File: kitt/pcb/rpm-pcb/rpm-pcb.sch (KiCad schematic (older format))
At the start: 155 parts, among them J1 Screw_Terminal_01x02, J2 Screw_Terminal_01x03, Q1 NDP6020P, Q2 NDP6020P, Q3 NDP6020P, Q4 NDP6020P, Q5 NDP6020P, Q6 NDP6020P, U1 TLC5940NT, U2 TLC5940NT, U3 TLC5940NT, U4 TLC5940NT, U5 TLC5940NT, U6 TLC5940NT, U7 TLC5940NT, U8 TLC5940NT, U9 TLC5940NT

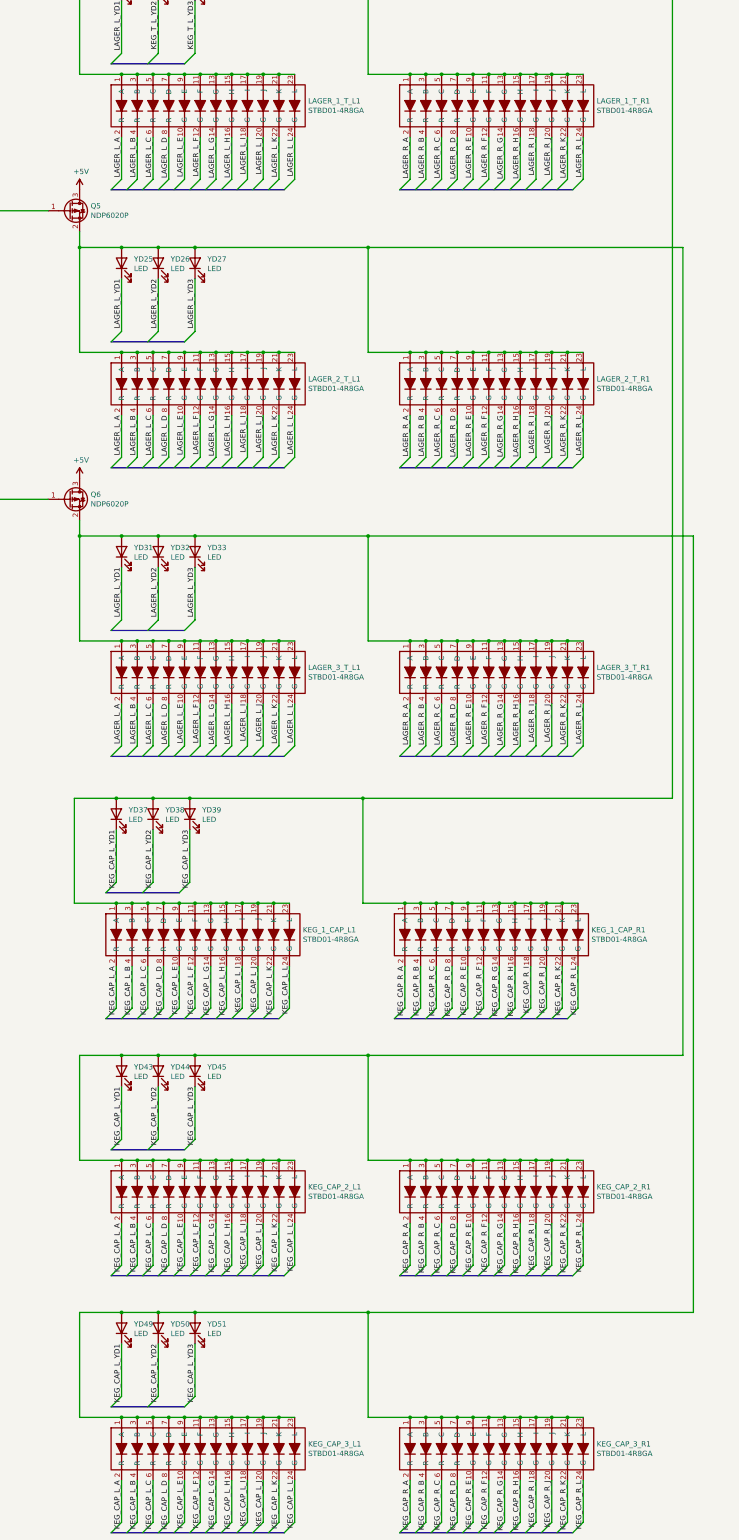
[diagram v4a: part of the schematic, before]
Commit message: fixed colors on bar displays
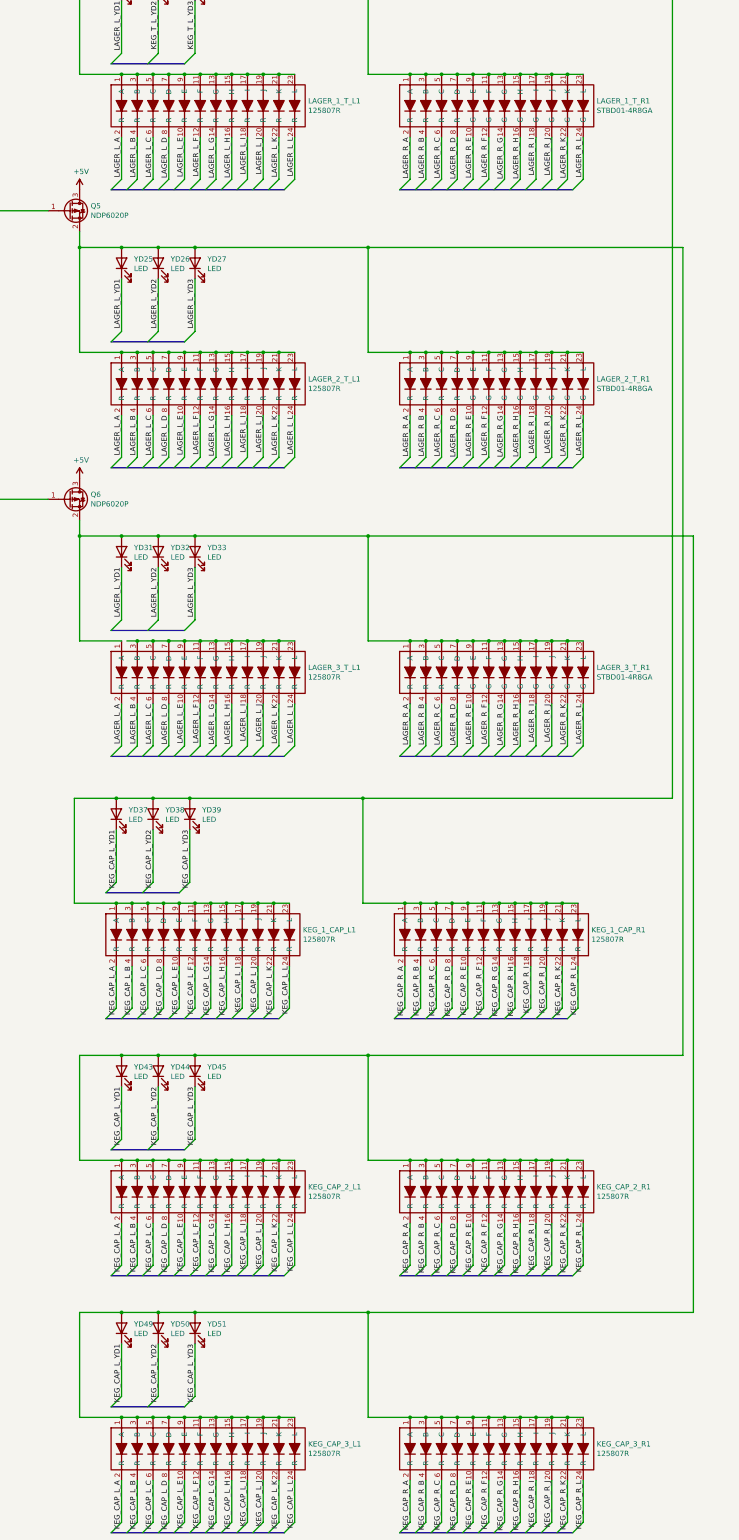
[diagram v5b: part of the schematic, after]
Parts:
- removed KEG_1_CAP_L1, KEG_1_CAP_R1, KEG_CAP_2_L1, KEG_CAP_2_R1, KEG_CAP_3_L1, KEG_CAP_3_R1, LAGER_1_T_L1, LAGER_2_T_L1, LAGER_3_T_L1: STBD01-4R8GA, symbol KITT-Symbols:STBD01-4R8GA
- added KEG_1_CAP_L1, KEG_1_CAP_R1, KEG_CAP_2_L1, KEG_CAP_2_R1, KEG_CAP_3_L1, KEG_CAP_3_R1, LAGER_1_T_L1, LAGER_2_T_L1, LAGER_3_T_L1: 125807R, symbol KITT-Symbols:125807R
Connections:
- net KEG_CAP_L_A: now also KEG_1_CAP_L1.2 (R), KEG_CAP_2_L1.2 (R), KEG_CAP_3_L1.2 (R)
- net KEG_CAP_L_B: now also KEG_1_CAP_L1.4 (R), KEG_CAP_2_L1.4 (R), KEG_CAP_3_L1.4 (R)
- net KEG_CAP_L_C: now also KEG_1_CAP_L1.6 (R), KEG_CAP_2_L1.6 (R), KEG_CAP_3_L1.6 (R)
- net KEG_CAP_L_D: now also KEG_1_CAP_L1.8 (R), KEG_CAP_2_L1.8 (R), KEG_CAP_3_L1.8 (R)
- net KEG_CAP_L_E: now also KEG_1_CAP_L1.10 (R), KEG_CAP_2_L1.10 (R), KEG_CAP_3_L1.10 (R)
- net KEG_CAP_L_F: now also KEG_1_CAP_L1.12 (R), KEG_CAP_2_L1.12 (R), KEG_CAP_3_L1.12 (R)
- net KEG_CAP_L_G: now also KEG_1_CAP_L1.14 (R), KEG_CAP_2_L1.14 (R), KEG_CAP_3_L1.14 (R)
- net KEG_CAP_L_H: now also KEG_1_CAP_L1.16 (R), KEG_CAP_2_L1.16 (R), KEG_CAP_3_L1.16 (R)
- net KEG_CAP_L_I: now also KEG_1_CAP_L1.18 (R), KEG_CAP_2_L1.18 (R), KEG_CAP_3_L1.18 (R)
- net KEG_CAP_L_J: now also KEG_1_CAP_L1.20 (R), KEG_CAP_2_L1.20 (R), KEG_CAP_3_L1.20 (R)
- net KEG_CAP_L_K: now also KEG_1_CAP_L1.22 (R), KEG_CAP_2_L1.22 (R), KEG_CAP_3_L1.22 (R)
- net KEG_CAP_L_L: now also KEG_1_CAP_L1.24 (R), KEG_CAP_2_L1.24 (R), KEG_CAP_3_L1.24 (R)
- net KEG_CAP_R_A: now also KEG_1_CAP_R1.2 (R), KEG_CAP_2_R1.2 (R), KEG_CAP_3_R1.2 (R)
- net KEG_CAP_R_B: now also KEG_1_CAP_R1.4 (R), KEG_CAP_2_R1.4 (R), KEG_CAP_3_R1.4 (R)
- net KEG_CAP_R_C: now also KEG_1_CAP_R1.6 (R), KEG_CAP_2_R1.6 (R), KEG_CAP_3_R1.6 (R)
- net KEG_CAP_R_D: now also KEG_1_CAP_R1.8 (R), KEG_CAP_2_R1.8 (R), KEG_CAP_3_R1.8 (R)
- net KEG_CAP_R_E: now also KEG_1_CAP_R1.10 (R), KEG_CAP_2_R1.10 (R), KEG_CAP_3_R1.10 (R)
- net KEG_CAP_R_F: now also KEG_1_CAP_R1.12 (R), KEG_CAP_2_R1.12 (R), KEG_CAP_3_R1.12 (R)
- net KEG_CAP_R_G: now also KEG_1_CAP_R1.14 (R), KEG_CAP_2_R1.14 (R), KEG_CAP_3_R1.14 (R)
- net KEG_CAP_R_H: now also KEG_1_CAP_R1.16 (R), KEG_CAP_2_R1.16 (R), KEG_CAP_3_R1.16 (R)
- net KEG_CAP_R_I: now also KEG_1_CAP_R1.18 (R), KEG_CAP_2_R1.18 (R), KEG_CAP_3_R1.18 (R)
- net KEG_CAP_R_J: now also KEG_1_CAP_R1.20 (R), KEG_CAP_2_R1.20 (R), KEG_CAP_3_R1.20 (R)
- net KEG_CAP_R_K: now also KEG_1_CAP_R1.22 (R), KEG_CAP_2_R1.22 (R), KEG_CAP_3_R1.22 (R)
- net KEG_CAP_R_L: now also KEG_1_CAP_R1.24 (R), KEG_CAP_2_R1.24 (R), KEG_CAP_3_R1.24 (R)
- net LAGER_L_A: now also LAGER_1_T_L1.2 (R), LAGER_2_T_L1.2 (R), LAGER_3_T_L1.2 (R)
- net LAGER_L_B: now also LAGER_1_T_L1.4 (R), LAGER_2_T_L1.4 (R), LAGER_3_T_L1.4 (R)
- net LAGER_L_C: now also LAGER_1_T_L1.6 (R), LAGER_2_T_L1.6 (R), LAGER_3_T_L1.6 (R)
- net LAGER_L_D: now also LAGER_1_T_L1.8 (R), LAGER_2_T_L1.8 (R), LAGER_3_T_L1.8 (R)
- net LAGER_L_E: now also LAGER_1_T_L1.10 (R), LAGER_2_T_L1.10 (R), LAGER_3_T_L1.10 (R)
- net LAGER_L_F: now also LAGER_1_T_L1.12 (R), LAGER_2_T_L1.12 (R), LAGER_3_T_L1.12 (R)
- net LAGER_L_G: now also LAGER_1_T_L1.14 (R), LAGER_2_T_L1.14 (R), LAGER_3_T_L1.14 (R)
- net LAGER_L_H: now also LAGER_1_T_L1.16 (R), LAGER_2_T_L1.16 (R), LAGER_3_T_L1.16 (R)
- net LAGER_L_I: now also LAGER_1_T_L1.18 (R), LAGER_2_T_L1.18 (R), LAGER_3_T_L1.18 (R)
- net LAGER_L_J: now also LAGER_1_T_L1.20 (R), LAGER_2_T_L1.20 (R), LAGER_3_T_L1.20 (R)
- net LAGER_L_K: now also LAGER_1_T_L1.22 (R), LAGER_2_T_L1.22 (R), LAGER_3_T_L1.22 (R)
- net LAGER_L_L: now also LAGER_1_T_L1.24 (R), LAGER_2_T_L1.24 (R), LAGER_3_T_L1.24 (R)
- net at LAGER_2_T_R1.1 (A), LAGER_2_T_R1.11 (F), LAGER_2_T_R1.13 (G)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: now also KEG_CAP_2_L1.1 (A), KEG_CAP_2_L1.11 (F), KEG_CAP_2_L1.13 (G), KEG_CAP_2_L1.15 (H), KEG_CAP_2_L1.17 (I), KEG_CAP_2_L1.19 (J), KEG_CAP_2_L1.21 (K), KEG_CAP_2_L1.23 (L), KEG_CAP_2_L1.3 (B), KEG_CAP_2_L1.5 (C), KEG_CAP_2_L1.7 (D), KEG_CAP_2_L1.9 (E), KEG_CAP_2_R1.1 (A), KEG_CAP_2_R1.11 (F), KEG_CAP_2_R1.13 (G), KEG_CAP_2_R1.15 (H), KEG_CAP_2_R1.17 (I), KEG_CAP_2_R1.19 (J), KEG_CAP_2_R1.21 (K), KEG_CAP_2_R1.23 (L), KEG_CAP_2_R1.3 (B), KEG_CAP_2_R1.5 (C), KEG_CAP_2_R1.7 (D), KEG_CAP_2_R1.9 (E), LAGER_2_T_L1.1 (A), LAGER_2_T_L1.11 (F), LAGER_2_T_L1.13 (G), LAGER_2_T_L1.15 (H), LAGER_2_T_L1.17 (I), LAGER_2_T_L1.19 (J), LAGER_2_T_L1.21 (K), LAGER_2_T_L1.23 (L), LAGER_2_T_L1.3 (B), LAGER_2_T_L1.5 (C), LAGER_2_T_L1.7 (D), LAGER_2_T_L1.9 (E)
- net at LAGER_3_T_R1.1 (A), LAGER_3_T_R1.11 (F), LAGER_3_T_R1.13 (G)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: now also KEG_CAP_3_L1.1 (A), KEG_CAP_3_L1.11 (F), KEG_CAP_3_L1.13 (G), KEG_CAP_3_L1.15 (H), KEG_CAP_3_L1.17 (I), KEG_CAP_3_L1.19 (J), KEG_CAP_3_L1.21 (K), KEG_CAP_3_L1.23 (L), KEG_CAP_3_L1.3 (B), KEG_CAP_3_L1.5 (C), KEG_CAP_3_L1.7 (D), KEG_CAP_3_L1.9 (E), KEG_CAP_3_R1.1 (A), KEG_CAP_3_R1.11 (F), KEG_CAP_3_R1.13 (G), KEG_CAP_3_R1.15 (H), KEG_CAP_3_R1.17 (I), KEG_CAP_3_R1.19 (J), KEG_CAP_3_R1.21 (K), KEG_CAP_3_R1.23 (L), KEG_CAP_3_R1.3 (B), KEG_CAP_3_R1.5 (C), KEG_CAP_3_R1.7 (D), KEG_CAP_3_R1.9 (E), LAGER_3_T_L1.1 (A)
- net at LAGER_1_T_R1.1 (A), LAGER_1_T_R1.11 (F), LAGER_1_T_R1.13 (G)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: now also KEG_1_CAP_L1.1 (A), KEG_1_CAP_L1.11 (F), KEG_1_CAP_L1.13 (G), KEG_1_CAP_L1.15 (H), KEG_1_CAP_L1.17 (I), KEG_1_CAP_L1.19 (J), KEG_1_CAP_L1.21 (K), KEG_1_CAP_L1.23 (L), KEG_1_CAP_L1.3 (B), KEG_1_CAP_L1.5 (C), KEG_1_CAP_L1.7 (D), KEG_1_CAP_L1.9 (E), KEG_1_CAP_R1.1 (A), KEG_1_CAP_R1.11 (F), KEG_1_CAP_R1.13 (G), KEG_1_CAP_R1.15 (H), KEG_1_CAP_R1.17 (I), KEG_1_CAP_R1.19 (J), KEG_1_CAP_R1.21 (K), KEG_1_CAP_R1.23 (L), KEG_1_CAP_R1.3 (B), KEG_1_CAP_R1.5 (C), KEG_1_CAP_R1.7 (D), KEG_1_CAP_R1.9 (E), LAGER_1_T_L1.1 (A), LAGER_1_T_L1.11 (F), LAGER_1_T_L1.13 (G), LAGER_1_T_L1.15 (H), LAGER_1_T_L1.17 (I), LAGER_1_T_L1.19 (J), LAGER_1_T_L1.21 (K), LAGER_1_T_L1.23 (L), LAGER_1_T_L1.3 (B), LAGER_1_T_L1.5 (C), LAGER_1_T_L1.7 (D), LAGER_1_T_L1.9 (E)
- new net: LAGER_3_T_L1.11 (F), LAGER_3_T_L1.13 (G), LAGER_3_T_L1.15 (H), LAGER_3_T_L1.17 (I), LAGER_3_T_L1.19 (J), LAGER_3_T_L1.21 (K), LAGER_3_T_L1.23 (L), LAGER_3_T_L1.3 (B), LAGER_3_T_L1.5 (C), LAGER_3_T_L1.7 (D), LAGER_3_T_L1.9 (E)

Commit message: fixed red and green bars
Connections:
- net KEG_T_L_A: now also KEG_1_T1.24 (G), KEG_2_T1.24 (G), KEG_3_T1.24 (G); no longer KEG_1_T1.2 (R), KEG_2_T1.2 (R), KEG_3_T1.2 (R)
- net KEG_T_L_B: now also KEG_1_T1.22 (G), KEG_2_T1.22 (G), KEG_3_T1.22 (G); no longer KEG_1_T1.4 (R), KEG_2_T1.4 (R), KEG_3_T1.4 (R)
- net KEG_T_L_C: now also KEG_1_T1.20 (G), KEG_2_T1.20 (G), KEG_3_T1.20 (G); no longer KEG_1_T1.6 (R), KEG_2_T1.6 (R), KEG_3_T1.6 (R)
- net KEG_T_L_D: now also KEG_1_T1.18 (G), KEG_2_T1.18 (G), KEG_3_T1.18 (G); no longer KEG_1_T1.8 (R), KEG_2_T1.8 (R), KEG_3_T1.8 (R)
- net KEG_T_L_E: now also KEG_1_T1.16 (G), KEG_2_T1.16 (G), KEG_3_T1.16 (G); no longer KEG_1_T1.10 (G), KEG_2_T1.10 (G), KEG_3_T1.10 (G)
- net KEG_T_L_F: now also KEG_1_T1.14 (G), KEG_2_T1.14 (G), KEG_3_T1.14 (G); no longer KEG_1_T1.12 (G), KEG_2_T1.12 (G), KEG_3_T1.12 (G)
- net KEG_T_L_G: now also KEG_1_T1.12 (G), KEG_2_T1.12 (G), KEG_3_T1.12 (G); no longer KEG_1_T1.14 (G), KEG_2_T1.14 (G), KEG_3_T1.14 (G)
- net KEG_T_L_H: now also KEG_1_T1.10 (G), KEG_2_T1.10 (G), KEG_3_T1.10 (G); no longer KEG_1_T1.16 (G), KEG_2_T1.16 (G), KEG_3_T1.16 (G)
- net KEG_T_L_I: now also KEG_1_T1.8 (R), KEG_2_T1.8 (R), KEG_3_T1.8 (R); no longer KEG_1_T1.18 (G), KEG_2_T1.18 (G), KEG_3_T1.18 (G)
- net KEG_T_L_J: now also KEG_1_T1.6 (R), KEG_2_T1.6 (R), KEG_3_T1.6 (R); no longer KEG_1_T1.20 (G), KEG_2_T1.20 (G), KEG_3_T1.20 (G)
- net KEG_T_L_K: now also KEG_1_T1.4 (R), KEG_2_T1.4 (R), KEG_3_T1.4 (R); no longer KEG_1_T1.22 (G), KEG_2_T1.22 (G), KEG_3_T1.22 (G)
- net KEG_T_L_L: now also KEG_1_T1.2 (R), KEG_2_T1.2 (R), KEG_3_T1.2 (R); no longer KEG_1_T1.24 (G), KEG_2_T1.24 (G), KEG_3_T1.24 (G)
- net KEG_T_R_A: now also KEG_4_T1.24 (G), KEG_5_T1.24 (G), LINE_T1.24 (G); no longer KEG_4_T1.2 (R), KEG_5_T1.2 (R), LINE_T1.2 (R)
- net KEG_T_R_B: now also KEG_4_T1.22 (G), KEG_5_T1.22 (G), LINE_T1.22 (G); no longer KEG_4_T1.4 (R), KEG_5_T1.4 (R), LINE_T1.4 (R)
- net KEG_T_R_C: now also KEG_4_T1.20 (G), KEG_5_T1.20 (G), LINE_T1.20 (G); no longer KEG_4_T1.6 (R), KEG_5_T1.6 (R), LINE_T1.6 (R)
- net KEG_T_R_D: now also KEG_4_T1.18 (G), KEG_5_T1.18 (G), LINE_T1.18 (G); no longer KEG_4_T1.8 (R), KEG_5_T1.8 (R), LINE_T1.8 (R)
- net KEG_T_R_E: now also KEG_4_T1.16 (G), KEG_5_T1.16 (G), LINE_T1.16 (G); no longer KEG_4_T1.10 (G), KEG_5_T1.10 (G), LINE_T1.10 (G)
- net KEG_T_R_F: now also KEG_4_T1.14 (G), KEG_5_T1.14 (G), LINE_T1.14 (G); no longer KEG_4_T1.12 (G), KEG_5_T1.12 (G), LINE_T1.12 (G)
- net KEG_T_R_G: now also KEG_4_T1.12 (G), KEG_5_T1.12 (G), LINE_T1.12 (G); no longer KEG_4_T1.14 (G), KEG_5_T1.14 (G), LINE_T1.14 (G)
- net KEG_T_R_H: now also KEG_4_T1.10 (G), KEG_5_T1.10 (G), LINE_T1.10 (G); no longer KEG_4_T1.16 (G), KEG_5_T1.16 (G), LINE_T1.16 (G)
- net KEG_T_R_I: now also KEG_4_T1.8 (R), KEG_5_T1.8 (R), LINE_T1.8 (R); no longer KEG_4_T1.18 (G), KEG_5_T1.18 (G), LINE_T1.18 (G)
- net KEG_T_R_J: now also KEG_4_T1.6 (R), KEG_5_T1.6 (R), LINE_T1.6 (R); no longer KEG_4_T1.20 (G), KEG_5_T1.20 (G), LINE_T1.20 (G)
- net KEG_T_R_K: now also KEG_4_T1.4 (R), KEG_5_T1.4 (R), LINE_T1.4 (R); no longer KEG_4_T1.22 (G), KEG_5_T1.22 (G), LINE_T1.22 (G)
- net KEG_T_R_L: now also KEG_4_T1.2 (R), KEG_5_T1.2 (R), LINE_T1.2 (R); no longer KEG_4_T1.24 (G), KEG_5_T1.24 (G), LINE_T1.24 (G)
- net LAGER_R_A: now also LAGER_1_T_R1.24 (G), LAGER_2_T_R1.24 (G), LAGER_3_T_R1.24 (G); no longer LAGER_1_T_R1.2 (R), LAGER_2_T_R1.2 (R), LAGER_3_T_R1.2 (R)
- net LAGER_R_B: now also LAGER_1_T_R1.22 (G), LAGER_2_T_R1.22 (G), LAGER_3_T_R1.22 (G); no longer LAGER_1_T_R1.4 (R), LAGER_2_T_R1.4 (R), LAGER_3_T_R1.4 (R)
- net LAGER_R_C: now also LAGER_1_T_R1.20 (G), LAGER_2_T_R1.20 (G), LAGER_3_T_R1.20 (G); no longer LAGER_1_T_R1.6 (R), LAGER_2_T_R1.6 (R), LAGER_3_T_R1.6 (R)
- net LAGER_R_D: now also LAGER_1_T_R1.18 (G), LAGER_2_T_R1.18 (G), LAGER_3_T_R1.18 (G); no longer LAGER_1_T_R1.8 (R), LAGER_2_T_R1.8 (R), LAGER_3_T_R1.8 (R)
- net LAGER_R_E: now also LAGER_1_T_R1.16 (G), LAGER_2_T_R1.16 (G), LAGER_3_T_R1.16 (G); no longer LAGER_1_T_R1.10 (G), LAGER_2_T_R1.10 (G), LAGER_3_T_R1.10 (G)
- net LAGER_R_F: now also LAGER_1_T_R1.14 (G), LAGER_2_T_R1.14 (G), LAGER_3_T_R1.14 (G); no longer LAGER_1_T_R1.12 (G), LAGER_2_T_R1.12 (G), LAGER_3_T_R1.12 (G)
- net LAGER_R_G: now also LAGER_1_T_R1.12 (G), LAGER_2_T_R1.12 (G), LAGER_3_T_R1.12 (G); no longer LAGER_1_T_R1.14 (G), LAGER_2_T_R1.14 (G), LAGER_3_T_R1.14 (G)
- net LAGER_R_H: now also LAGER_1_T_R1.10 (G), LAGER_2_T_R1.10 (G), LAGER_3_T_R1.10 (G); no longer LAGER_1_T_R1.16 (G), LAGER_2_T_R1.16 (G), LAGER_3_T_R1.16 (G)
- net LAGER_R_I: now also LAGER_1_T_R1.8 (R), LAGER_2_T_R1.8 (R), LAGER_3_T_R1.8 (R); no longer LAGER_1_T_R1.18 (G), LAGER_2_T_R1.18 (G), LAGER_3_T_R1.18 (G)
- net LAGER_R_J: now also LAGER_1_T_R1.6 (R), LAGER_2_T_R1.6 (R), LAGER_3_T_R1.6 (R); no longer LAGER_1_T_R1.20 (G), LAGER_2_T_R1.20 (G), LAGER_3_T_R1.20 (G)
- net LAGER_R_K: now also LAGER_1_T_R1.4 (R), LAGER_2_T_R1.4 (R), LAGER_3_T_R1.4 (R); no longer LAGER_1_T_R1.22 (G), LAGER_2_T_R1.22 (G), LAGER_3_T_R1.22 (G)
- net LAGER_R_L: now also LAGER_1_T_R1.2 (R), LAGER_2_T_R1.2 (R), LAGER_3_T_R1.2 (R); no longer LAGER_1_T_R1.24 (G), LAGER_2_T_R1.24 (G), LAGER_3_T_R1.24 (G)

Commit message: sed to get flangeless led
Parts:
- CG1, CG10, CG11, CG12, CG13, CG14, CG15, CG16, CG17, CG18, CG19, CG2, CG20, CG21, CG3, CG4, CG5, CG6, CG7, CG8, CG9, CG_22, CG_23, CG_24, CG_25, CG_26, CG_27, CG_28, CG_29, CG_30, YD1, YD10, YD11, YD12, YD13, YD14, YD15, YD16, YD17, YD18, YD19, YD2, YD20, YD21, YD25, YD26, YD27, YD3, YD31, YD32, YD33, YD37, YD38, YD39, YD4, YD43, YD44, YD45, YD49, YD5, YD50, YD51, YD6, YD7, YD8, YD9: footprint (none) -> KITT-Footpads:Flangeless_LED

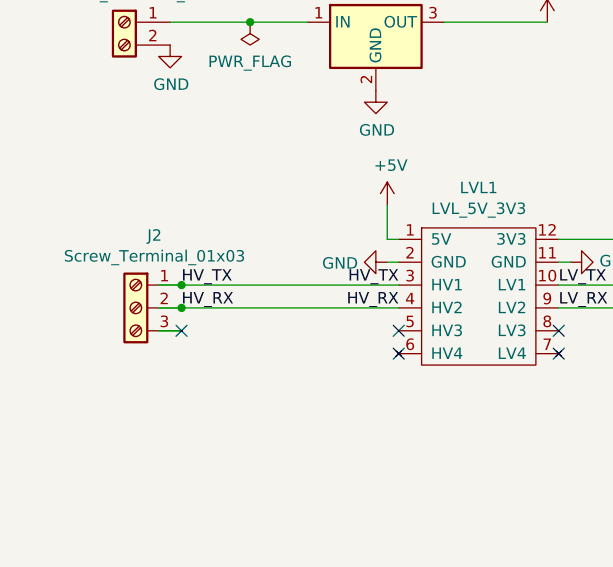
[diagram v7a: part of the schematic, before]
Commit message: added footpads for light blocks and screw terminals
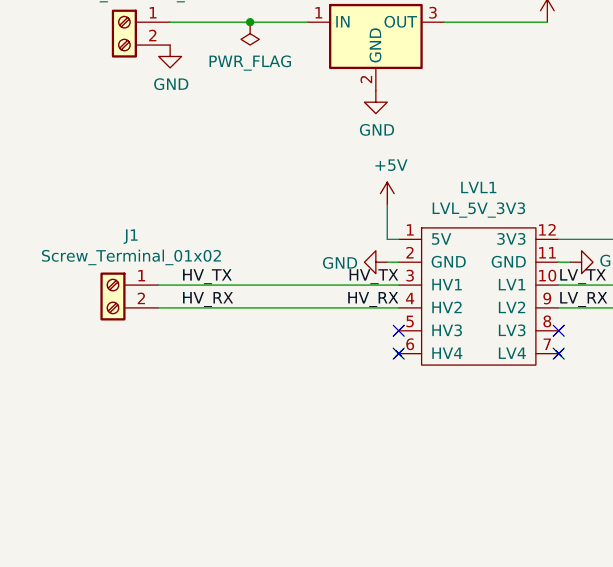
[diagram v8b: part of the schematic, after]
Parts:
- removed J2: Screw_Terminal_01x03, symbol Connector:Screw_Terminal_01x03
- added J1: Screw_Terminal_01x02, KITT-Footpads:5mm_Screw_Terminal_01x02, symbol Connector:Screw_Terminal_01x02
- J1: footprint (none) -> KITT-Footpads:5mm_Screw_Terminal_01x02
- RPM1, RPM2, RPM3: footprint (none) -> KITT-Footpads:KB2855SGD_Light_Square
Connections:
- net HV_RX: now also J1.2 (Pin_2)
- net HV_TX: now also J1.1 (Pin_1)
- no-connect marks 42 -> 41
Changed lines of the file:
@@
 NoConn ~ 3800 21050
 NoConn ~ 3100 21050
-NoConn ~ 2150 21050
 Text Label 5500 17600 1    50   ~ 0
 CT_DISP1_A
@@
 Wire Wire Line
 	3800 20650 5100 20650
-Wire Wire Line
-	2150 21050 2050 21050
-Wire Wire Line
-	2150 20950 3100 20950
-Connection ~ 2150 20950
-Wire Wire Line
-	2150 20850 3100 20850
-Connection ~ 2150 20850
-$Comp
-L Connector:Screw_Terminal_01x03 J2
-U 1 1 612893C8
-P 1950 20950
-F 0 "J2" H 1868 21267 50  0000 C CNN
-F 1 "Screw_Terminal_01x03" H 1868 21176 50  0000 C CNN
-F 2 "" H 1950 20950 50  0001 C CNN
-F 3 "~" H 1950 20950 50  0001 C CNN
-	1    1950 20950
-	-1   0    0    -1
-$EndComp
 Connection ~ 12500 5100
 $Comp
@@
 F 0 "RPM3" H 13228 5796 50  0000 L CNN
 F 1 "KB2855SGD" H 13228 5705 50  0000 L CNN
-F 2 "" H 12400 5850 50  0001 C CNN
+F 2 "KITT-Footpads:KB2855SGD_Light_Square" H 12400 5850 50  0001 C CNN
 F 3 "" H 12400 5850 50  0001 C CNN
 	1    12800 5750
@@
 F 0 "RPM2" H 11928 5796 50  0000 L CNN
 F 1 "KB2855SGD" H 11928 5705 50  0000 L CNN
-F 2 "" H 11100 5850 50  0001 C CNN
+F 2 "KITT-Footpads:KB2855SGD_Light_Square" H 11100 5850 50  0001 C CNN
 F 3 "" H 11100 5850 50  0001 C CNN
 	1    11500 5750
@@
 F 0 "RPM1" H 10628 5796 50  0000 L CNN
 F 1 "KB2855SGD" H 10628 5705 50  0000 L CNN
-F 2 "" H 9800 5850 50  0001 C CNN
+F 2 "KITT-Footpads:KB2855SGD_Light_Square" H 9800 5850 50  0001 C CNN
 F 3 "" H 9800 5850 50  0001 C CNN
 	1    10200 5750
@@
 F 0 "J1" H 1818 19917 50  0000 C CNN
 F 1 "Screw_Terminal_01x02" H 1818 19826 50  0000 C CNN
-F 2 "" H 1900 19700 50  0001 C CNN
+F 2 "KITT-Footpads:5mm_Screw_Terminal_01x02" H 1900 19700 50  0001 C CNN
 F 3 "~" H 1900 19700 50  0001 C CNN
 	1    1900 19700
@@
 	1    0    0    -1
 $EndComp
-Wire Wire Line
-	2050 20850 2150 20850
-Wire Wire Line
-	2050 20950 2150 20950
 Text Label 2150 20850 0    50   ~ 0
 HV_TX
@@
 Wire Wire Line
 	25550 7850 25700 7850
+Connection ~ 25550 7850
 Wire Bus Line
 	21150 10250 21850 10250
@@
 Wire Bus Line
 	5400 16700 17300 16700
-Connection ~ 25550 7850
+Wire Wire Line
+	2050 20850 3100 20850
+Wire Wire Line
+	2050 20950 3100 20950
+$Comp
+L Connector:Screw_Terminal_01x02 J1
+U 1 1 61430C56
+P 1850 20850
+F 0 "J1" H 1768 21067 50  0000 C CNN
+F 1 "Screw_Terminal_01x02" H 1768 20976 50  0000 C CNN
+F 2 "KITT-Footpads:5mm_Screw_Terminal_01x02" H 1850 20850 50  0001 C CNN
+F 3 "~" H 1850 20850 50  0001 C CNN
+	1    1850 20850
+	-1   0    0    -1
+$EndComp
 $EndSCHEMATC
